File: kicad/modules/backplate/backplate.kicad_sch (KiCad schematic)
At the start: 1 part, among them J1 10018784-10210TLF

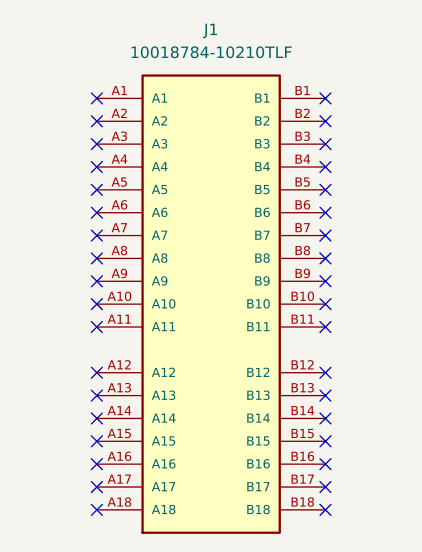
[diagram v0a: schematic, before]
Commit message: update backplate libraries and schematic
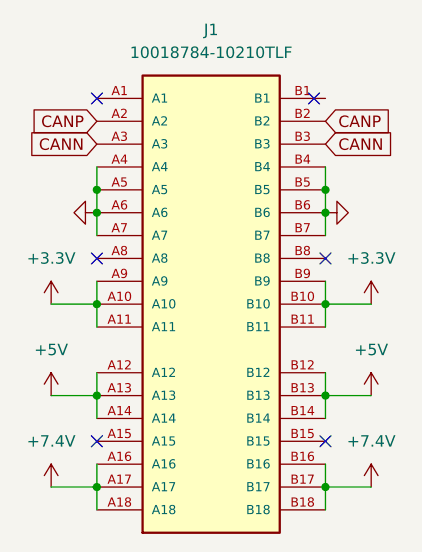
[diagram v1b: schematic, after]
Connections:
- net +3.3V: now reaches J1.A10
- net +3.3V: now also J1.A11, J1.A9, J1.B10, J1.B11, J1.B9
- net +5V: now reaches J1.A12
- net +5V: now also J1.A13, J1.A14, J1.B12, J1.B13, J1.B14
- net +7.4V: now reaches J1.A16
- net +7.4V: now also J1.A17, J1.A18, J1.B16, J1.B17, J1.B18
- net CANP: now reaches J1.A2
- net CANP: now also J1.B2
- net CANN: now reaches J1.A3
- net CANN: now also J1.B3
- net GND: now reaches J1.A4
- net GND: now also J1.A5, J1.A6, J1.A7, J1.B4, J1.B5, J1.B6, J1.B7
- no-connect marks 36 -> 6

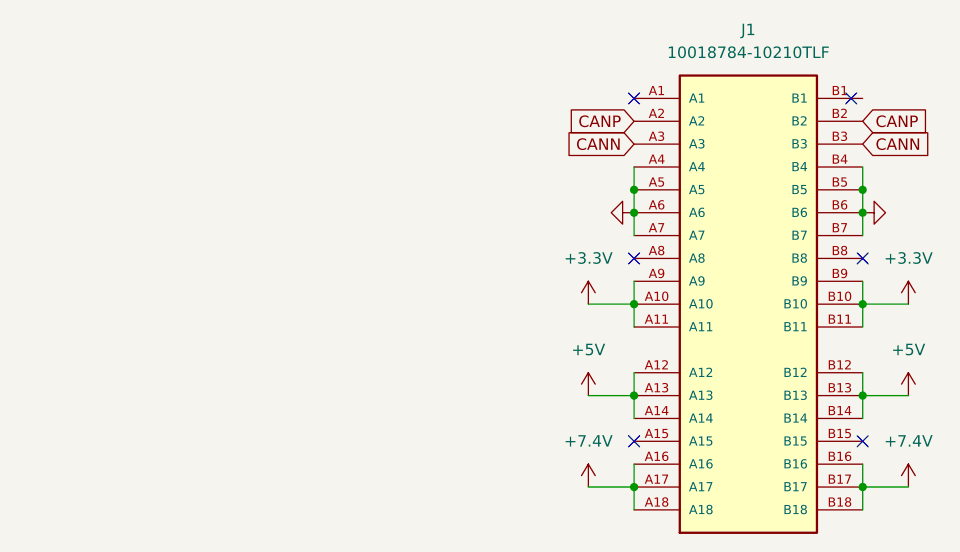
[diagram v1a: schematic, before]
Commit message: update PCIe footprint; delete holes, and pads
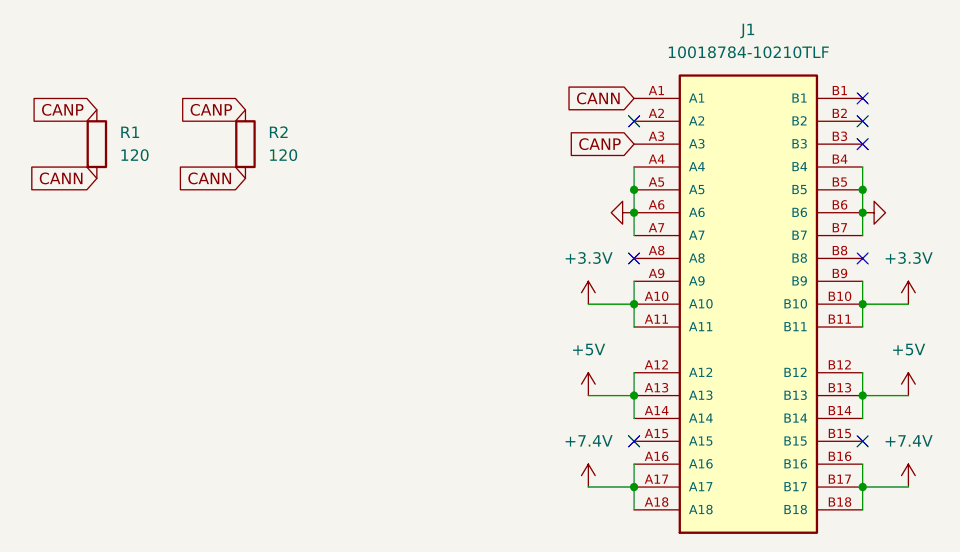
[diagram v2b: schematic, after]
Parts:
- added R1, R2: 120, Resistor_SMD:R_0805_2012Metric, symbol Device:R
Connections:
- net CANN: now also J1.A1, R1.2, R2.2; no longer J1.A3, J1.B3
- net CANP: now also J1.A3, R1.1, R2.1; no longer J1.A2, J1.B2
- no-connect marks 6 -> 8
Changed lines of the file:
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@@
 	)
 	(no_connect
-		(at 139.7 66.04)
+		(at 140.97 66.04)
+	)
+	(no_connect
+		(at 115.57 68.58)
 	)
 	(no_connect
@@
 	)
 	(no_connect
-		(at 115.57 66.04)
+		(at 140.97 68.58)
 	)
 	(no_connect
@@
 	)
 	(no_connect
+		(at 140.97 71.12)
+	)
+	(no_connect
 		(at 115.57 104.14)
 	)
@@
 		)
 	)
+	(global_label "CANP"
+		(shape input)
+		(at 55.88 67.31 180)
+		(fields_autoplaced yes)
+		(effects
+			(font
+				(size 1.27 1.27)
+			)
+			(justify right)
+		)
+		(property "Intersheetrefs" "${INTERSHEET_REFS}"
+			(at 47.9357 67.31 0)
+			(effects
+				(font
+					(size 1.27 1.27)
+				)
+				(justify right)
+				(hide yes)
+			)
+		)
+	)
 	(global_label "CANN"
+		(shape input)
+		(at 115.57 66.04 180)
+		(fields_autoplaced yes)
+		(effects
+			(font
+				(size 1.27 1.27)
+			)
+			(justify right)
+		)
+		(property "Intersheetrefs" "${INTERSHEET_REFS}"
+			(at 107.5652 66.04 0)
+			(effects
+				(font
+					(size 1.27 1.27)
+				)
+				(justify right)
+				(hide yes)
+			)
+		)
+	)
+	(global_label "CANP"
 		(shape input)
 		(at 115.57 71.12 180)
@@
 		)
 		(property "Intersheetrefs" "${INTERSHEET_REFS}"
-			(at 107.5652 71.12 0)
+			(at 107.6257 71.12 0)
 			(effects
 				(font
@@
 	(global_label "CANP"
 		(shape input)
-		(at 115.57 68.58 180)
+		(at 72.39 67.31 180)
 		(fields_autoplaced yes)
 		(effects
@@
 		)
 		(property "Intersheetrefs" "${INTERSHEET_REFS}"
-			(at 107.6257 68.58 0)
+			(at 64.4457 67.31 0)
 			(effects
 				(font
@@
 		)
 	)
-	(global_label "CANP"
+	(global_label "CANN"
 		(shape input)
-		(at 140.97 68.58 0)
+		(at 55.88 74.93 180)
 		(fields_autoplaced yes)
 		(effects
@@
 				(size 1.27 1.27)
 			)
-			(justify left)
+			(justify right)
 		)
 		(property "Intersheetrefs" "${INTERSHEET_REFS}"
-			(at 148.9143 68.58 0)
-			(effects
-				(font
-					(size 1.27 1.27)
-				)
-				(justify left)
+			(at 47.8752 74.93 0)
+			(effects
+				(font
+					(size 1.27 1.27)
+				)
+				(justify right)
 				(hide yes)
 			)
@@
 	(global_label "CANN"
 		(shape input)
-		(at 140.97 71.12 0)
+		(at 72.39 74.93 180)
 		(fields_autoplaced yes)
 		(effects
@@
 				(size 1.27 1.27)
 			)
-			(justify left)
+			(justify right)
 		)
 		(property "Intersheetrefs" "${INTERSHEET_REFS}"
-			(at 148.9748 71.12 0)
-			(effects
-				(font
-					(size 1.27 1.27)
-				)
-				(justify left)
+			(at 64.3852 74.93 0)
+			(effects
+				(font
+					(size 1.27 1.27)
+				)
+				(justify right)
 				(hide yes)
 			)
@@
 	)
 	(symbol
+		(lib_id "Device:R")
+		(at 55.88 71.12 0)
+		(unit 1)
+		(exclude_from_sim no)
+		(in_bom yes)
+		(on_board yes)
+		(dnp no)
+		(fields_autoplaced yes)
+		(property "Reference" "R1"
+			(at 58.42 69.8499 0)
+			(effects
+				(font
+					(size 1.27 1.27)
+				)
+				(justify left)
+			)
+		)
+		(property "Value" "120"
+			(at 58.42 72.3899 0)
+			(effects
+				(font
+					(size 1.27 1.27)
+				)
+				(justify left)
+			)
+		)
+		(property "Footprint" "Resistor_SMD:R_0805_2012Metric"
+			(at 54.102 71.12 90)
+			(effects
+				(font
+					(size 1.27 1.27)
+				)
+				(hide yes)
+			)
+		)
+		(property "Datasheet" "~"
+			(at 55.88 71.12 0)
+			(effects
+				(font
+					(size 1.27 1.27)
+				)
+				(hide yes)
+			)
+		)
+		(property "Description" "Resistor"
+			(at 55.88 71.12 0)
+			(effects
+				(font
+					(size 1.27 1.27)
+				)
+				(hide yes)
+			)
+		)
+		(pin "1"
+		)
+		(pin "2"
+		)
+		(instances
+			(project ""
+				(path "/3ac1a34a-3a2d-4f8e-be23-a5fa61208278"
+					(reference "R1")
+					(unit 1)
+				)
+			)
+		)
+	)
+	(symbol
 		(lib_id "power:VAA")
 		(at 110.49 88.9 0)
@@
 					(unit 1)
 				)
+			)
+		)
+	)
+	(symbol
+		(lib_id "Device:R")
+		(at 72.39 71.12 0)
+		(unit 1)
+		(exclude_from_sim no)
+		(in_bom yes)
+		(on_board yes)
+		(dnp no)
+		(fields_autoplaced yes)
+		(property "Reference" "R2"
+			(at 74.93 69.8499 0)
+			(effects
+				(font
+					(size 1.27 1.27)
+				)
+				(justify left)
+			)
+		)
+		(property "Value" "120"
+			(at 74.93 72.3899 0)
+			(effects
+				(font
+					(size 1.27 1.27)
+				)
+				(justify left)
+			)
+		)
+		(property "Footprint" "Resistor_SMD:R_0805_2012Metric"
+			(at 70.612 71.12 90)
+			(effects
+				(font
+					(size 1.27 1.27)
+				)
+				(hide yes)
+			)
+		)
+		(property "Datasheet" "~"
+			(at 72.39 71.12 0)
+			(effects
+				(font
+					(size 1.27 1.27)
+				)
+				(hide yes)
+			)
+		)
+		(property "Description" "Resistor"
+			(at 72.39 71.12 0)
+			(effects
+				(font
+					(size 1.27 1.27)
+				)
+				(hide yes)
+			)
+		)
+		(pin "1"
+		)
+		(pin "2"
+		)
+		(instances
+			(project "backplate"
+				(path "/3ac1a34a-3a2d-4f8e-be23-a5fa61208278"
+					(reference "R2")
+					(unit 1)
+				)
